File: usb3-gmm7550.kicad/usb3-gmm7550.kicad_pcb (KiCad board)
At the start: 4 copper layers, 75 x 50 mm, 202 parts, among them J1 USB_C_Receptacle, J2 USB_C_Receptacle_USB2.0, J3 SWD, J4 10144517-061802LF, J5 10144517-061802LF, J6 DNI, Q1 NX6008NBK, Q2 NX6008NBK, Q3 NX6008NBK, Q4 STL9P3LLH6, Q5 STL9P3LLH6, Q6 STL9P3LLH6, SW1 SW_Push, SW2 SW_Push, SW3 SW_Push, SW4 SW_Push, SW5 SW_Push, U1 ECMF4-40A100N10, U10 74LVC1G07, U11 INA180A2, U12 AP7330, U13 AP7330, U14 IS25LP016D-JNLE, U15 ECMF02-2AMX6, U16 LM4040DBZ-3, U17 RP2040, U18 STUSB1600, U19 LM66200DRLR, U2 ECMF4-40A100N10, U3 ECMF02-2AMX6, U4 AP7330, U5 TUSB542, U6 SN65LVDS4RSER, U7 USB3340, U8 STUSB03E, U9 SiP32510, Y1 445I23D12M00000

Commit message: Placement -- work in progress
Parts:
- removed JP1: Conn_02x02_Odd_Even, Connector_PinHeader_2.54mm:PinHeader_2x02_P2.54mm_Vertical
- added R89: 15, Resistor_SMD:R_0402_1005Metric, F.Cu at (97.7, 40.6)
- added R90: 15, Resistor_SMD:R_0402_1005Metric, F.Cu at (97.7, 42.5)
- added SW6: SW_DIP_x02, Button_Switch_SMD:SW_DIP_SPSTx02_Slide_Omron_A6H-2101_W6.15mm_P1.27mm, F.Cu at (79.3, 52.5)
- R46, R47, R48, R49, R68: footprint Resistor_SMD:R_0603_1608Metric -> Resistor_SMD:R_0402_1005Metric
- moved C52 99.4 mm to (63.8, 68.0), turned to 180 degrees
- moved C55 94.6 mm to (69.7, 65.3), turned to 90 degrees
- moved C50 92.3 mm to (69.8, 81.3), turned to 90 degrees
- moved R68 91.8 mm to (67.2, 52.1), turned to 90 degrees
- moved R82 89.8 mm to (63.3, 69.6), turned to 180 degrees
- moved R84 82.3 mm to (71.0, 72.0), turned to 90 degrees
- moved R48 82.1 mm to (87.8, 95.5), turned to -90 degrees
- moved R49 80.1 mm to (89.3, 95.5), turned to -90 degrees
- moved R72 76.8 mm to (70.0, 85.3)
- moved R15 76.6 mm to (110.5, 82.2), turned to -90 degrees
- moved R14 74.9 mm to (110.5, 80.3)
- moved R73 74.9 mm to (71.9, 85.3)
- moved R75 73.6 mm to (73.3, 84.2)
- moved U8 72.5 mm to (121.1, 70.6)
- moved R5 72.4 mm to (77.1, 87.0), turned to 0 degrees
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
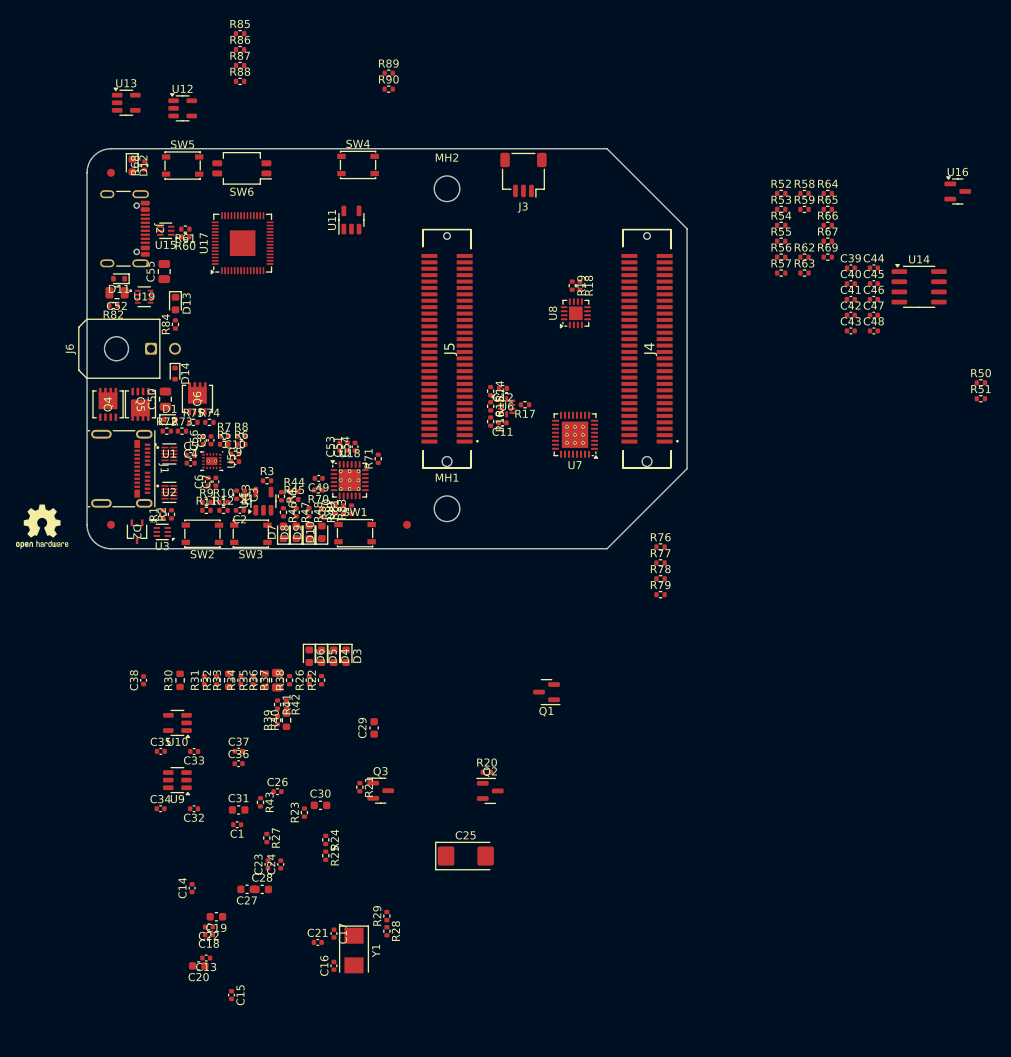
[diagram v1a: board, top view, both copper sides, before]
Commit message: Preliminary placement is ready
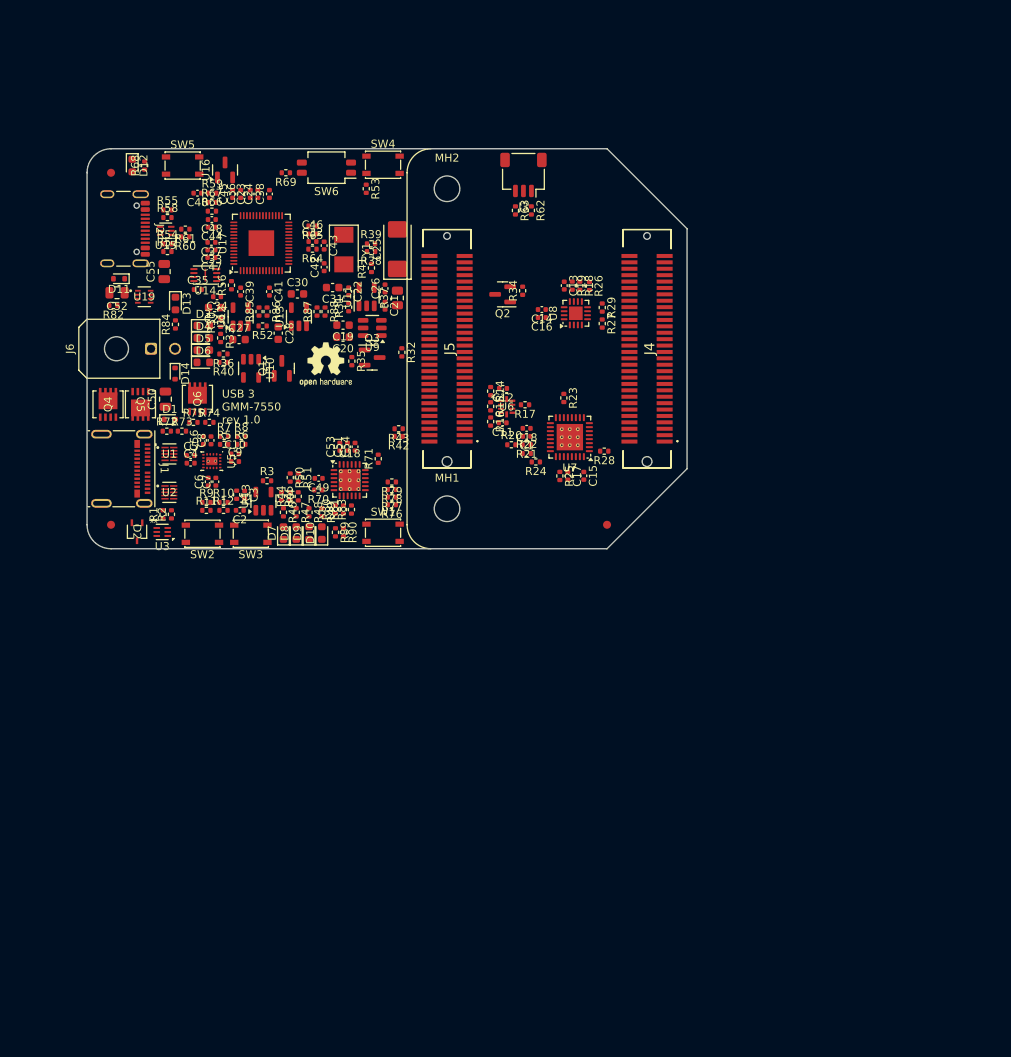
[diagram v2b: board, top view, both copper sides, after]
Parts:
- R30, R33, R36, R40: footprint Resistor_SMD:R_0603_1608Metric -> Resistor_SMD:R_0402_1005Metric
- U14: value IS25LP016D-JNLE -> MX25R1635FZU; footprint Package_SO:SOIC-8_3.9x4.9mm_P1.27mm -> Package_SON:Winbond_USON-8-1EP_3x2mm_P0.5mm_EP0.2x1.6mm
- moved C13 95.2 mm to (119.7, 67.1), turned to -90 degrees
- moved U16 91.6 mm to (77.2, 52.6), turned to 90 degrees
- moved U14 89.2 mm to (74.8, 65.8), turned to 180 degrees
- moved Y1 87.6 mm to (92.1, 62.6)
- moved R50 87.1 mm to (85.4, 91.1), turned to -90 degrees
- moved R51 85.9 mm to (86.4, 91.1), turned to -90 degrees
- moved C16 85.1 mm to (116.8, 71.1), turned to 180 degrees
- moved C14 84.5 mm to (116.8, 70.1), turned to 180 degrees
- moved C48 83.9 mm to (75.6, 58.9), turned to 180 degrees
- moved C24 83.9 mm to (81.3, 55.6)
- moved C23 83.8 mm to (80.4, 55.6)
- moved C47 83.1 mm to (75.5, 63.6), turned to 180 degrees
- moved C44 82.9 mm to (75.6, 59.8), turned to 180 degrees
- moved C40 82.5 mm to (73.8, 55.5), turned to 180 degrees
- moved C22 81.3 mm to (92.7, 67.8), turned to -90 degrees
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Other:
- board text added: "USB 3 GMM-7550 rev 1.0"

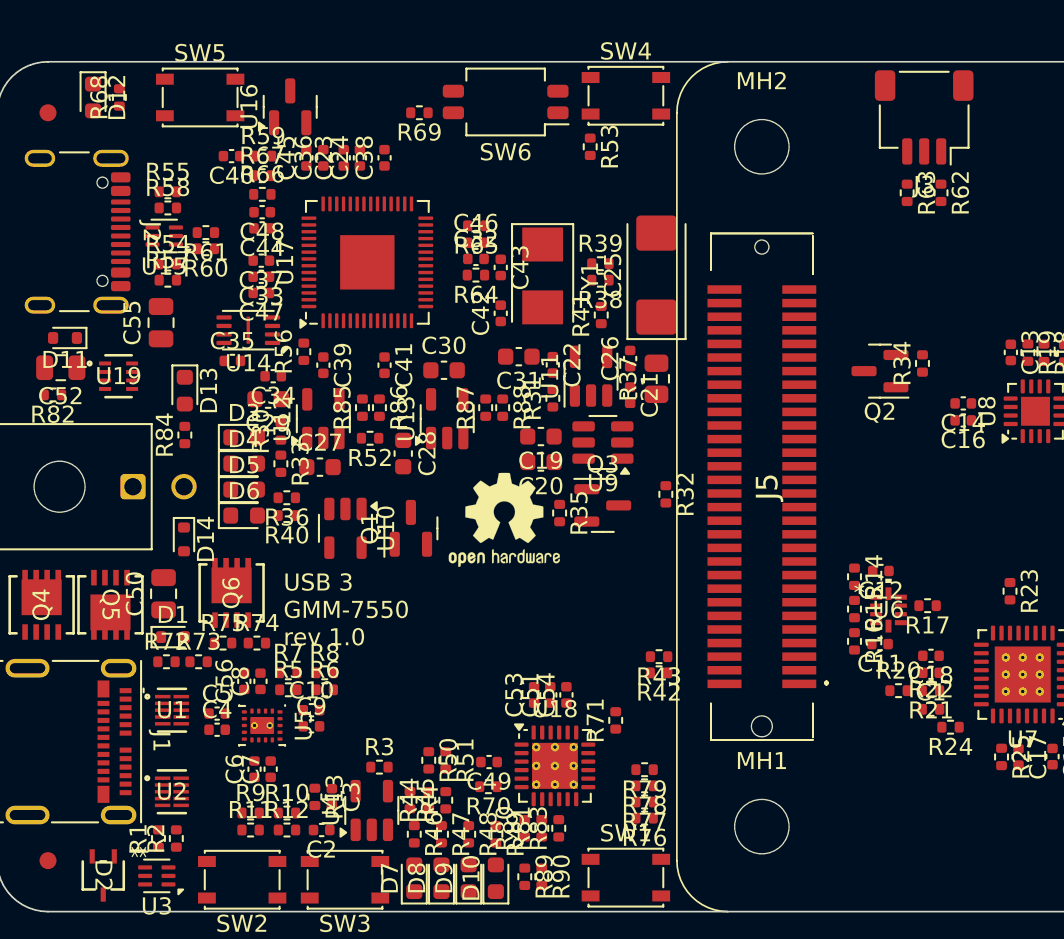
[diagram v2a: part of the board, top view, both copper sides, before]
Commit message: Connect USB 3 SuperSpeed diff. pairs
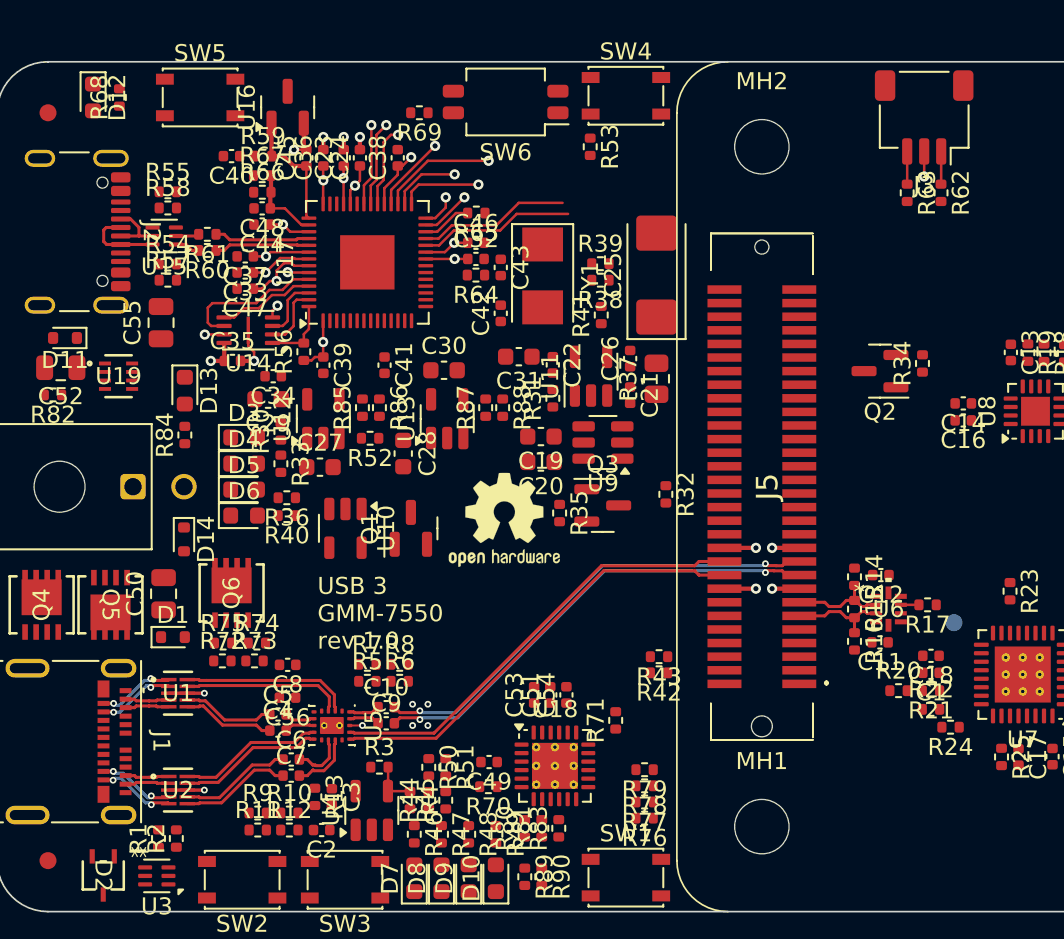
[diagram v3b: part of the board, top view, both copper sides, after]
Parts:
- added TP1: TestPoint, TestPoint:TestPoint_Pad_D1.0mm, B.Cu at (116.3, 83.0)
- moved R5 4.68 mm to (81.8, 86.5)
- moved R7 4.68 mm to (81.8, 85.5)
- moved R6 4.44 mm to (83.7, 86.5)
- moved R8 4.44 mm to (83.7, 85.5)
- moved C10 4.40 mm to (82.9, 88.0)
- moved C9 4.40 mm to (82.9, 88.9)
- moved U5 4.10 mm to (79.7, 89.0)
- moved C4 3.58 mm to (76.5, 89.3)
- moved C5 3.58 mm to (76.5, 88.4)
- moved R72 3.29 mm to (73.3, 85.2)
- moved R73 3.29 mm to (75.2, 85.2)
- moved C56 2.72 mm to (77.1, 87.4), turned to 180 degrees
- moved C6 2.23 mm to (77.3, 91.0), turned to 0 degrees
- moved C8 1.87 mm to (77.1, 85.5), turned to 180 degrees
- moved C7 1.27 mm to (77.3, 92.0), turned to 0 degrees
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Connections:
- net Net-(J1-RX1+) renamed /USB3/J1_R1_P
- net Net-(J1-RX1-) renamed /USB3/J1_R1_N
- net Net-(J1-TX1+) renamed /USB3/J1_T1_P
- net Net-(J1-TX1-) renamed /USB3/J1_T1_N
- net Net-(U1-D1+1) renamed /USB3/R1_P
- net Net-(U1-D1-1) renamed /USB3/R1_N
- net Net-(U1-D2+1) renamed /USB3/T1C_P
- net Net-(U1-D2-1) renamed /USB3/T1C_N
- net Net-(U15-D+_in) renamed /RP2040/U15_D_P
- net Net-(U15-D+_out) renamed /RP2040/J2_D_P
- net Net-(U15-D-_in) renamed /RP2040/U15_D_N
- net Net-(U15-D-_out) renamed /RP2040/J2_D_N
- net Net-(U17-USB_DM) renamed /RP2040/RP_D_N
- net Net-(U17-USB_DP) renamed /RP2040/RP_D_P
- net Net-(U3-D+_out) renamed /USB3/J1_D_P
- net Net-(U3-D-_out) renamed /USB3/J1_D_N
- net Net-(U5-RX_AP+) renamed /USB3/APR_P
- net Net-(U5-RX_AP-) renamed /USB3/APR_N
- net Net-(U5-Tx_Con_1+) renamed /USB3/T1_P
- net Net-(U5-Tx_Con_1-) renamed /USB3/T1_N
- net Net-(U5-Tx_Con_2+) renamed /USB3/T2_P
- net Net-(U5-Tx_Con_2-) renamed /USB3/T2_N
- C10 pad 2: AP_RX_P -> AP_RX_N
- C6 pad 1: Net-(U2-D2-1) -> /USB3/T2C_N
- C7 pad 1: Net-(U2-D2+1) -> /USB3/T2C_P
- C9 pad 2: AP_RX_N -> AP_RX_P
- J1 pad A10: Net-(J1-RX2-) -> /USB3/J1_R2_N
- J1 pad A11: Net-(J1-RX2+) -> /USB3/J1_R2_P
- J1 pad B2: Net-(J1-TX2+) -> /USB3/J1_T2_P
- J1 pad B3: Net-(J1-TX2-) -> /USB3/J1_T2_N
- U1 pad 8: unconnected-(U1-GND1-Pad8) -> GND
- U2 pad 1: Net-(J1-RX2+) -> /USB3/J1_R2_N
- U2 pad 10: Net-(U2-D1+1) -> /USB3/R2_N
- U2 pad 2: Net-(J1-RX2-) -> /USB3/J1_R2_P
- U2 pad 4: Net-(J1-TX2+) -> /USB3/J1_T2_N
- U2 pad 5: Net-(J1-TX2-) -> /USB3/J1_T2_P
- U2 pad 6: Net-(U2-D2-1) -> /USB3/T2C_P
- U2 pad 7: Net-(U2-D2+1) -> /USB3/T2C_N
- U2 pad 8: unconnected-(U2-GND1-Pad8) -> GND
- U2 pad 9: Net-(U2-D1-1) -> /USB3/R2_P
- U5 pad 14: AP_TX_N -> AP_TX_P
- U5 pad 15: AP_TX_P -> AP_TX_N
- U5 pad 8: Net-(U2-D1-1) -> /USB3/R2_N
- U5 pad 9: Net-(U2-D1+1) -> /USB3/R2_P
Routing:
- net AP_RX_N: track 0.00 -> 27.8 mm, vias 0 -> 2
- net AP_RX_P: track 0.00 -> 27.8 mm, vias 0 -> 2
- net AP_TX_N: track 0.00 -> 26.3 mm
- net AP_TX_P: track 0.00 -> 26.3 mm
- net GND: track 0.00 -> 20.8 mm, vias 0 -> 17
- net +2V5: track 0.00 -> 17.2 mm, vias 0 -> 6
- net /USB3/R1_P: track 0.00 -> 10.0 mm
- net /USB3/R1_N: track 0.00 -> 9.51 mm
- net +1V1: track 0.00 -> 9.46 mm, vias 0 -> 3
- net Net-(U17-SWCLK): track 0.00 -> 9.14 mm
- net Net-(U17-SWD): track 0.00 -> 8.92 mm
- net /USB3/R2_N: track 0.00 -> 8.57 mm
- net /USB3/R2_P: track 0.00 -> 8.57 mm
- net /RP2040/RP_QSPI_SCLK: track 0.00 -> 8.56 mm
- net /RP2040/ADC_AVDD: track 0.00 -> 7.35 mm
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- added copper zone on In1.Cu, net GND

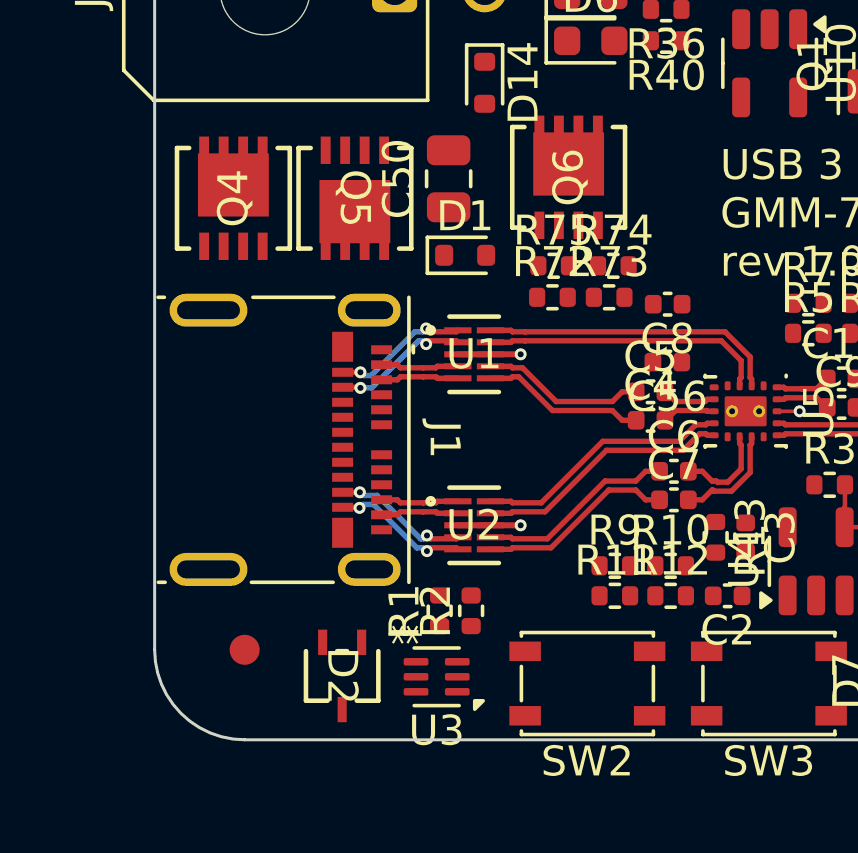
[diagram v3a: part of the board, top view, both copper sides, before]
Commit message: Layout: break-out J1 (target USB Type-C)
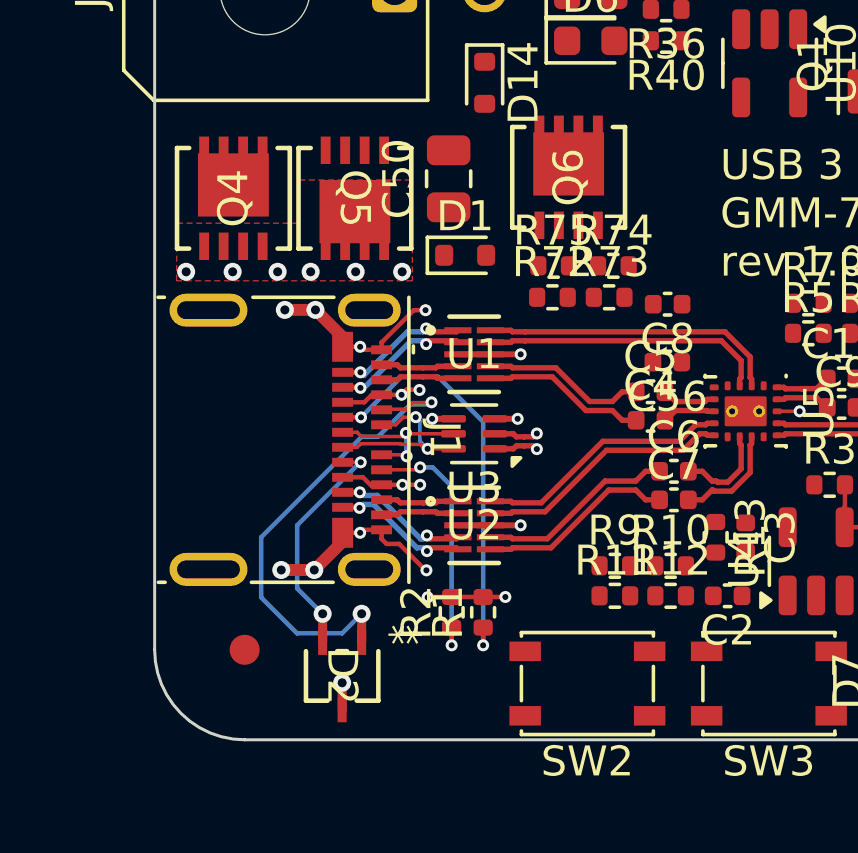
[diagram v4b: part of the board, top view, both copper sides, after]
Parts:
- moved U3 8.20 mm to (70.7, 89.8)
- moved R1 1.45 mm to (71.0, 95.8)
- moved R2 0.65 mm to (69.9, 95.8)
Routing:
- net GND: track 20.8 -> 38.2 mm, vias 17 -> 30
- net CON_CC1: track 0.00 -> 16.4 mm, vias 0 -> 2
- net Net-(J1-SBU2): track 0.00 -> 14.0 mm, vias 0 -> 2
- net Net-(J1-SBU1): track 0.00 -> 8.52 mm, vias 0 -> 2
- net CON_CC2: track 0.00 -> 7.85 mm, vias 0 -> 2
- net /USB3/J1_D_P: track 0.00 -> 6.29 mm, vias 0 -> 2
- net /USB3/J1_D_N: track 0.00 -> 5.47 mm, vias 0 -> 2
- net VBUS_TRGT: track 0.00 -> 5.46 mm, vias 0 -> 10
- net USB2_D_N: track 0.00 -> 1.49 mm, vias 0 -> 1
- net USB2_D_P: track 0.00 -> 1.49 mm, vias 0 -> 1
- added copper zone on F.Cu, net VBUS_TRGT
